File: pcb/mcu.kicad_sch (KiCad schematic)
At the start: 23 parts, among them J1 AVR-ISP-6, U15 TL431DBZ, U6 ATmega328P-AU, Y1 14.7456 MHz

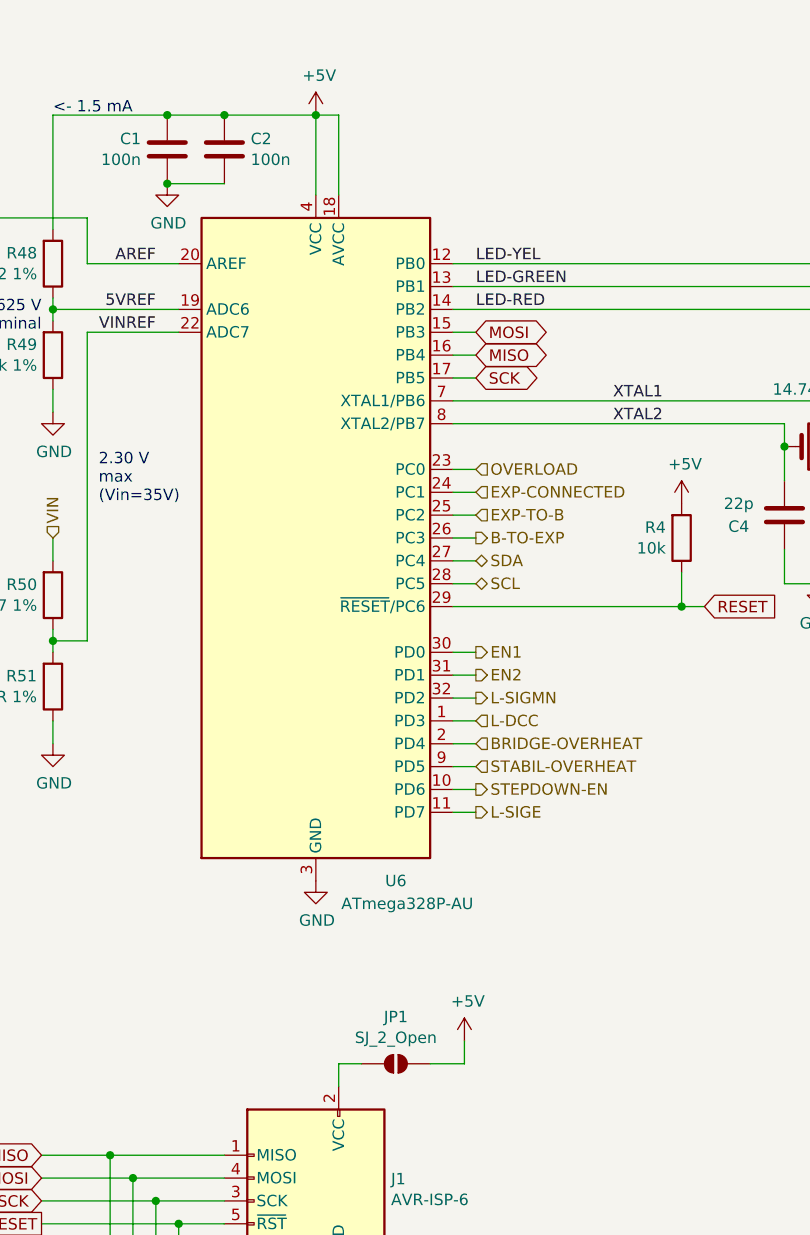
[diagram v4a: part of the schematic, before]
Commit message: Add stabil heatsinks, minor improvements.
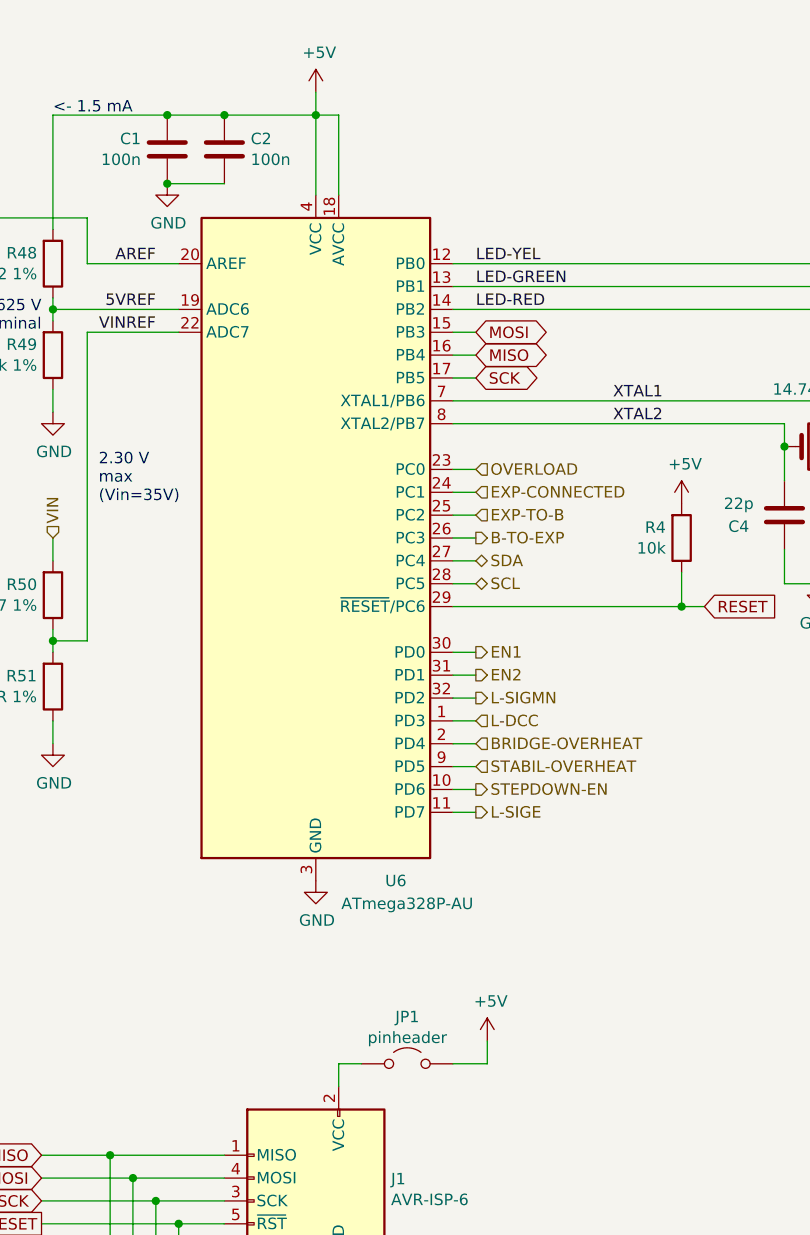
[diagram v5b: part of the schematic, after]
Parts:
- JP1: value SJ_2_Open -> pinheader; footprint Jumper:SolderJumper-2_P1.3mm_Open_RoundedPad1.0x1.5mm -> Connector_PinHeader_2.54mm:PinHeader_1x02_P2.54mm_Vertical; symbol Jumper:SolderJumper_2_Open -> Jumper:Jumper_2_Open
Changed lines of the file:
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@@
 	(wire
 		(pts
+			(xy 137.16 31.75) (xy 137.16 34.29)
+		)
+		(stroke
+			(width 0)
+			(type default)
+		)
+	)
+	(wire
+		(pts
 			(xy 107.95 92.71) (xy 107.95 93.98)
 		)
@@
 	(wire
 		(pts
-			(xy 153.67 139.7) (xy 149.86 139.7)
-		)
-		(stroke
-			(width 0)
-			(type default)
-		)
-	)
-	(wire
-		(pts
 			(xy 223.52 80.01) (xy 223.52 77.47)
 		)
@@
 	(wire
 		(pts
-			(xy 153.67 137.16) (xy 153.67 139.7)
+			(xy 156.21 137.16) (xy 156.21 139.7)
 		)
 		(stroke
@@
 	(wire
 		(pts
+			(xy 152.4 139.7) (xy 156.21 139.7)
+		)
+		(stroke
+			(width 0)
+			(type default)
+		)
+	)
+	(wire
+		(pts
 			(xy 106.68 152.4) (xy 116.84 152.4)
 		)
@@
 	)
 	(symbol
-		(lib_id "Jumper:SolderJumper_2_Open")
-		(at 146.05 139.7 0)
+		(lib_id "Jumper:Jumper_2_Open")
+		(at 147.32 139.7 0)
 		(mirror y)
 		(unit 1)
-		(exclude_from_sim no)
+		(exclude_from_sim yes)
 		(in_bom yes)
 		(on_board yes)
 		(dnp no)
 		(property "Reference" "JP1"
-			(at 146.05 134.493 0)
+			(at 147.32 134.493 0)
 			(effects
 				(font
@@
 			)
 		)
-		(property "Value" "SJ_2_Open"
-			(at 146.05 136.8044 0)
+		(property "Value" "pinheader"
+			(at 147.32 136.8044 0)
 			(effects
 				(font
@@
 			)
 		)
-		(property "Footprint" "Jumper:SolderJumper-2_P1.3mm_Open_RoundedPad1.0x1.5mm"
-			(at 146.05 139.7 0)
+		(property "Footprint" "Connector_PinHeader_2.54mm:PinHeader_1x02_P2.54mm_Vertical"
+			(at 147.32 139.7 0)
 			(effects
 				(font
@@
 		)
 		(property "Datasheet" "~"
-			(at 146.05 139.7 0)
+			(at 147.32 139.7 0)
 			(effects
 				(font
@@
 			)
 		)
-		(property "Description" "Solder Jumper, 2-pole, open"
-			(at 146.05 139.7 0)
+		(property "Description" "Jumper, 2-pole, open"
+			(at 147.32 139.7 0)
 			(effects
 				(font
@@
 	(symbol
 		(lib_id "power:+5V")
-		(at 137.16 34.29 0)
+		(at 137.16 31.75 0)
 		(unit 1)
 		(exclude_from_sim no)
@@
 		(dnp no)
 		(property "Reference" "#PWR0110"
-			(at 137.16 38.1 0)
+			(at 137.16 35.56 0)
 			(effects
 				(font
@@
 		)
 		(property "Value" "+5V"
-			(at 137.541 29.8958 0)
+			(at 137.541 27.3558 0)
 			(effects
 				(font
@@
 		)
 		(property "Footprint" ""
-			(at 137.16 34.29 0)
+			(at 137.16 31.75 0)
 			(effects
 				(font
@@
 		)
 		(property "Datasheet" ""
-			(at 137.16 34.29 0)
+			(at 137.16 31.75 0)
 			(effects
 				(font
@@
 		)
 		(property "Description" "Power symbol creates a global label with name \"+5V\""
-			(at 137.16 34.29 0)
+			(at 137.16 31.75 0)
 			(effects
 				(font
@@
 	(symbol
 		(lib_id "power:+5V")
-		(at 153.67 137.16 0)
+		(at 156.21 137.16 0)
 		(unit 1)
 		(exclude_from_sim no)
@@
 		(dnp no)
 		(property "Reference" "#PWR0112"
-			(at 153.67 140.97 0)
+			(at 156.21 140.97 0)
 			(effects
 				(font
@@
 		)
 		(property "Value" "+5V"
-			(at 154.051 132.7658 0)
+			(at 156.591 132.7658 0)
 			(effects
 				(font
@@
 		)
 		(property "Footprint" ""
-			(at 153.67 137.16 0)
+			(at 156.21 137.16 0)
 			(effects
 				(font
@@
 		)
 		(property "Datasheet" ""
-			(at 153.67 137.16 0)
+			(at 156.21 137.16 0)
 			(effects
 				(font
@@
 		)
 		(property "Description" "Power symbol creates a global label with name \"+5V\""
-			(at 153.67 137.16 0)
+			(at 156.21 137.16 0)
 			(effects
 				(font

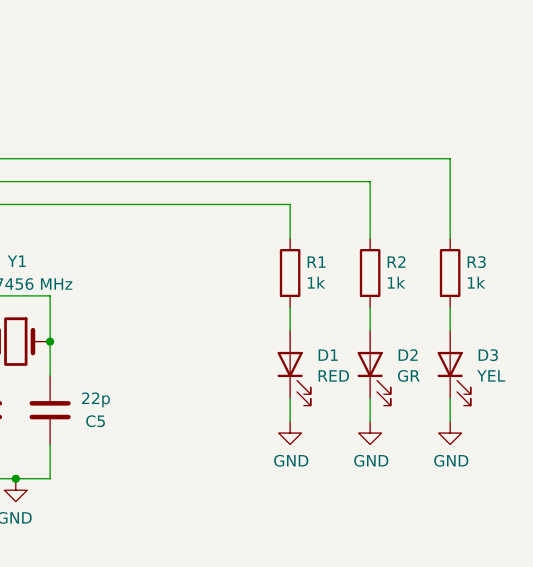
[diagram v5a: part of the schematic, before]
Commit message: Use polyfuse instead of resistor for main-exp protection.
Make voltage measurement possible.
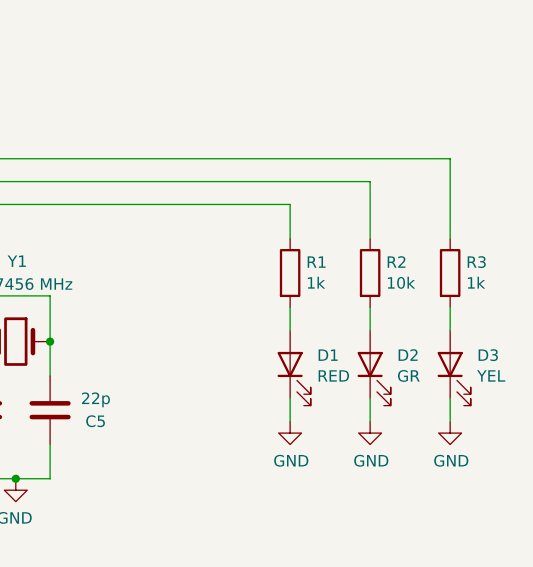
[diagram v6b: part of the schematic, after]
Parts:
- R2: value 1k -> 10k
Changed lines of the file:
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@@
 			)
 		)
-		(property "Value" "1k"
+		(property "Value" "10k"
 			(at 234.188 64.643 0)
 			(effects

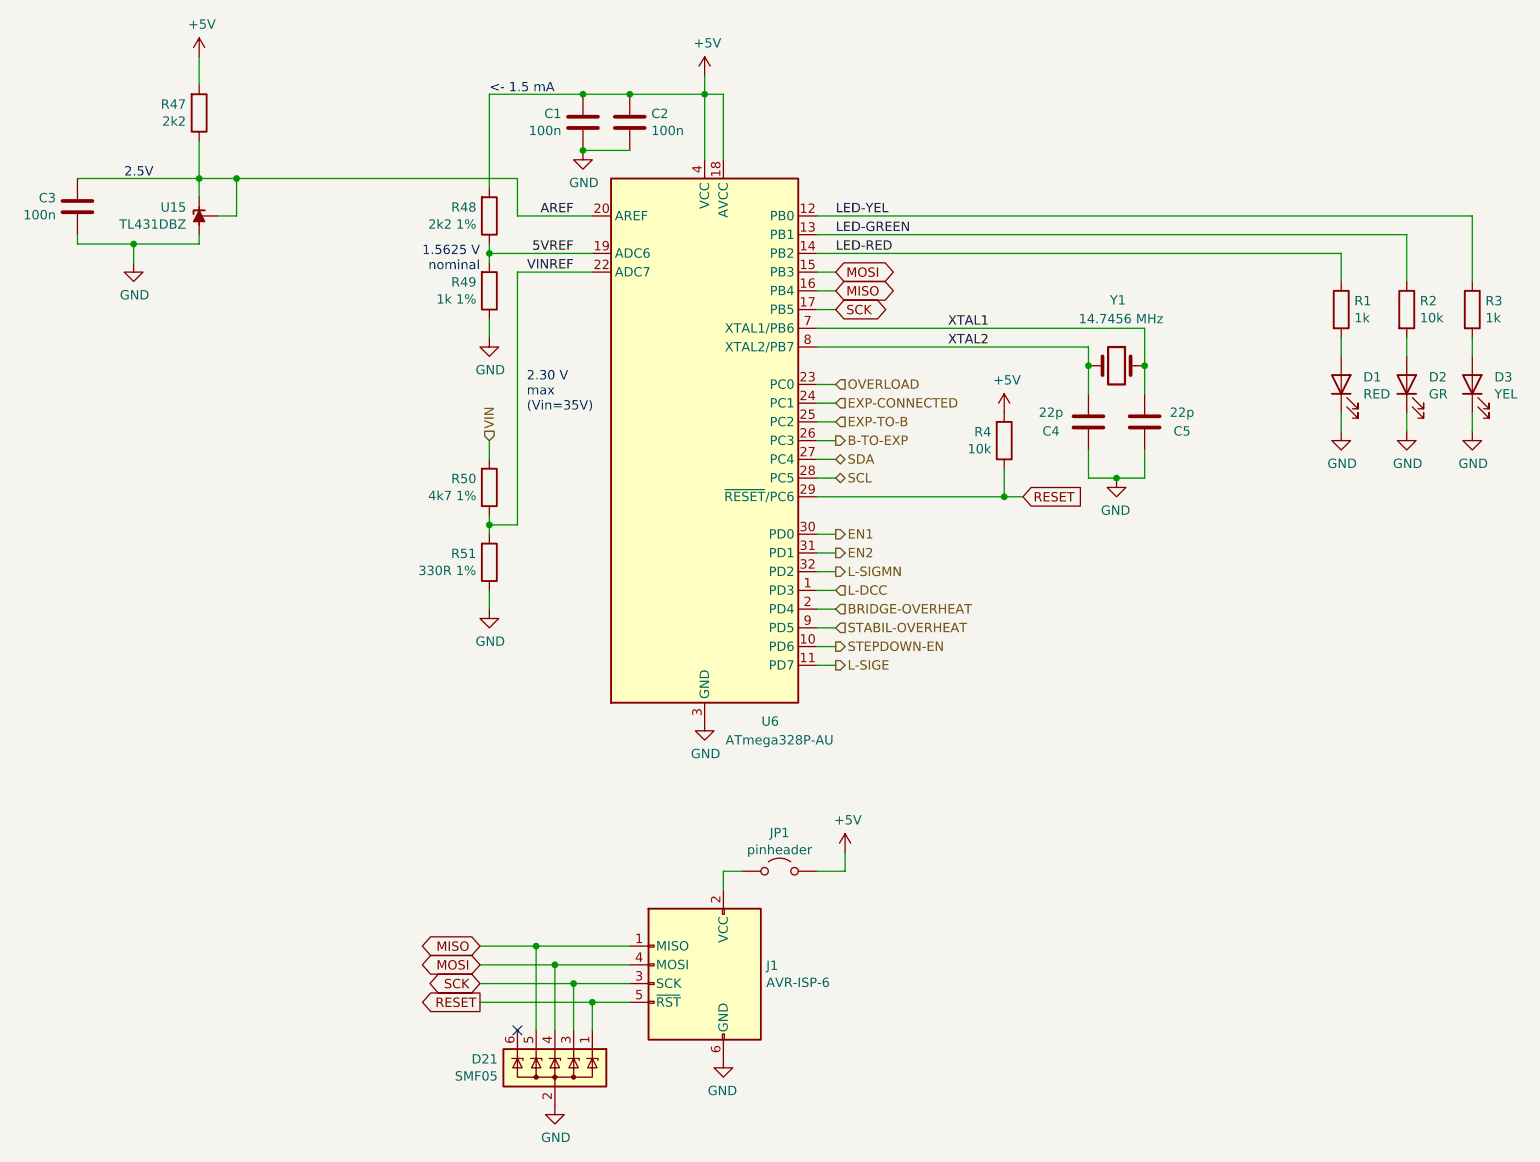
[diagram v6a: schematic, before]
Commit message: Use ATmega328pb instead of ATmega328p.
Reason: obtain some free pins as a reserve.
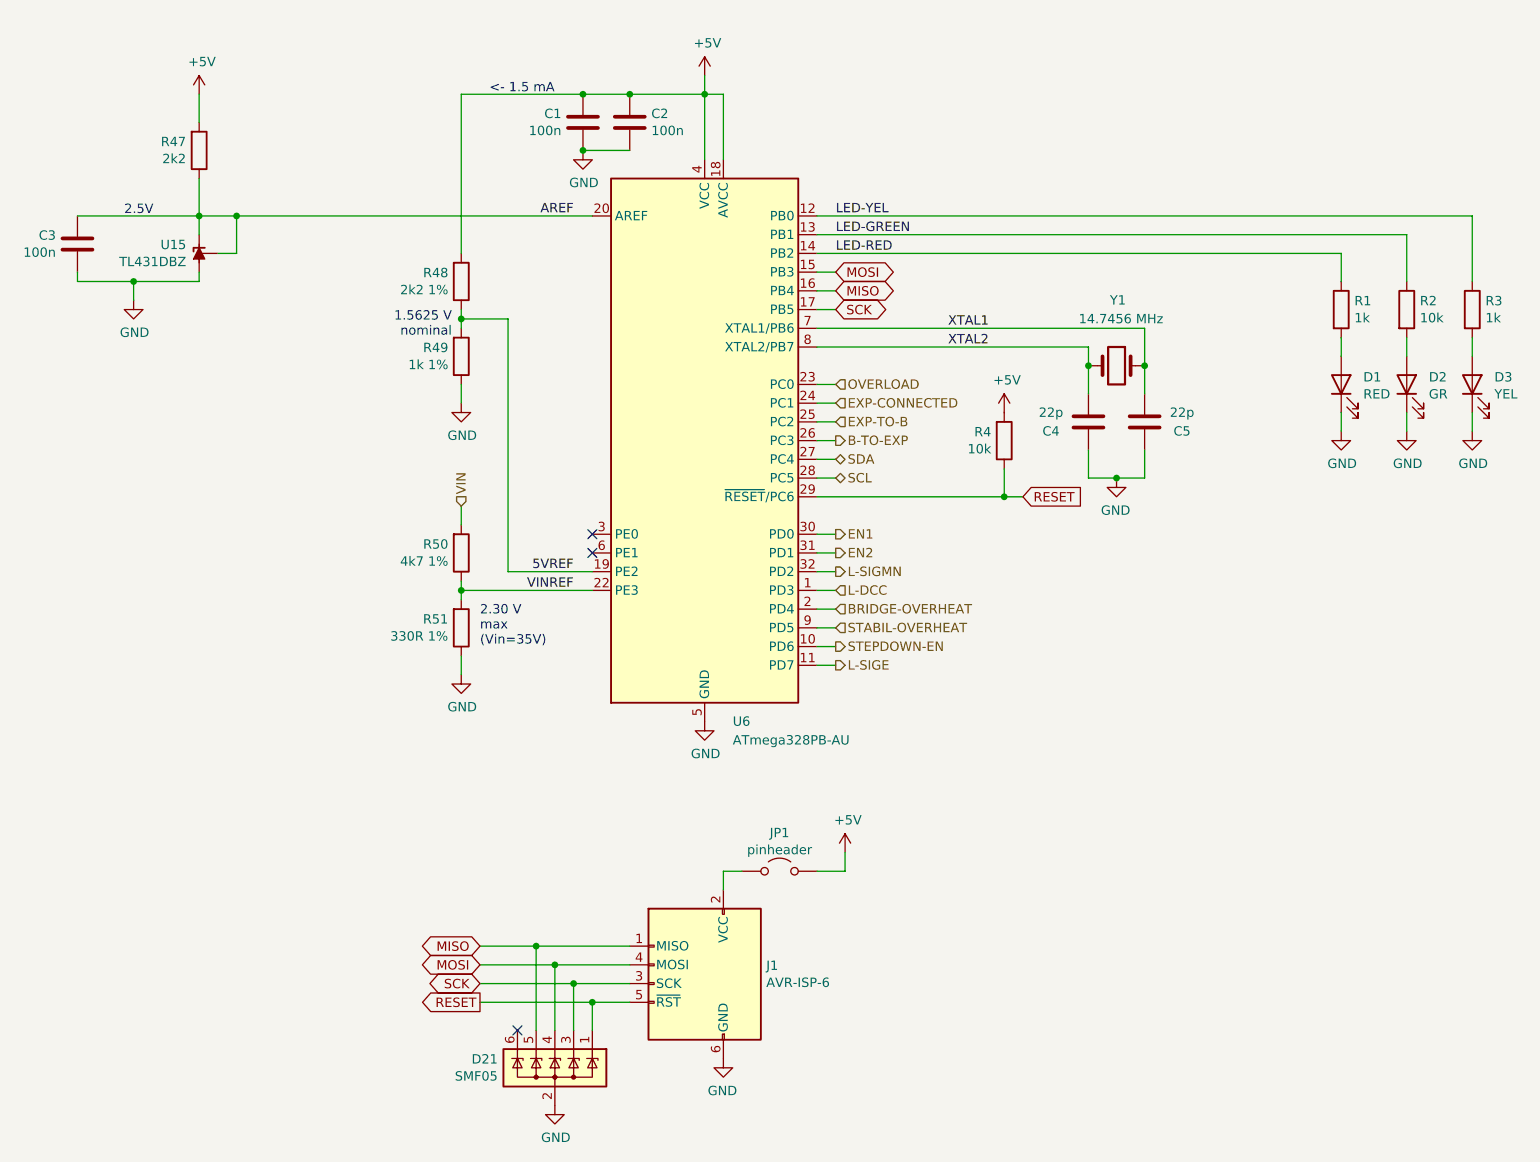
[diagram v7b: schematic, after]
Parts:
- U6: value ATmega328P-AU -> ATmega328PB-AU; symbol MCU_Microchip_ATmega:ATmega328P-A -> MCU_Microchip_ATmega:ATmega328PB-A
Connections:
- net +5V: no longer U6.6 (VCC)
- net GND: no longer U6.3 (GND)
- no-connect marks 1 -> 3
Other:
- moved on the sheet: C3, R47, R48, R49, R50, R51, U15
